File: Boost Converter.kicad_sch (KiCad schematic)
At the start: 21 parts, among them IC1 AHV85110KNHTR, J1 Array, J2 Battery, Q1 IGL65R080D2XUMA1, U1 Nucleo_L432KC

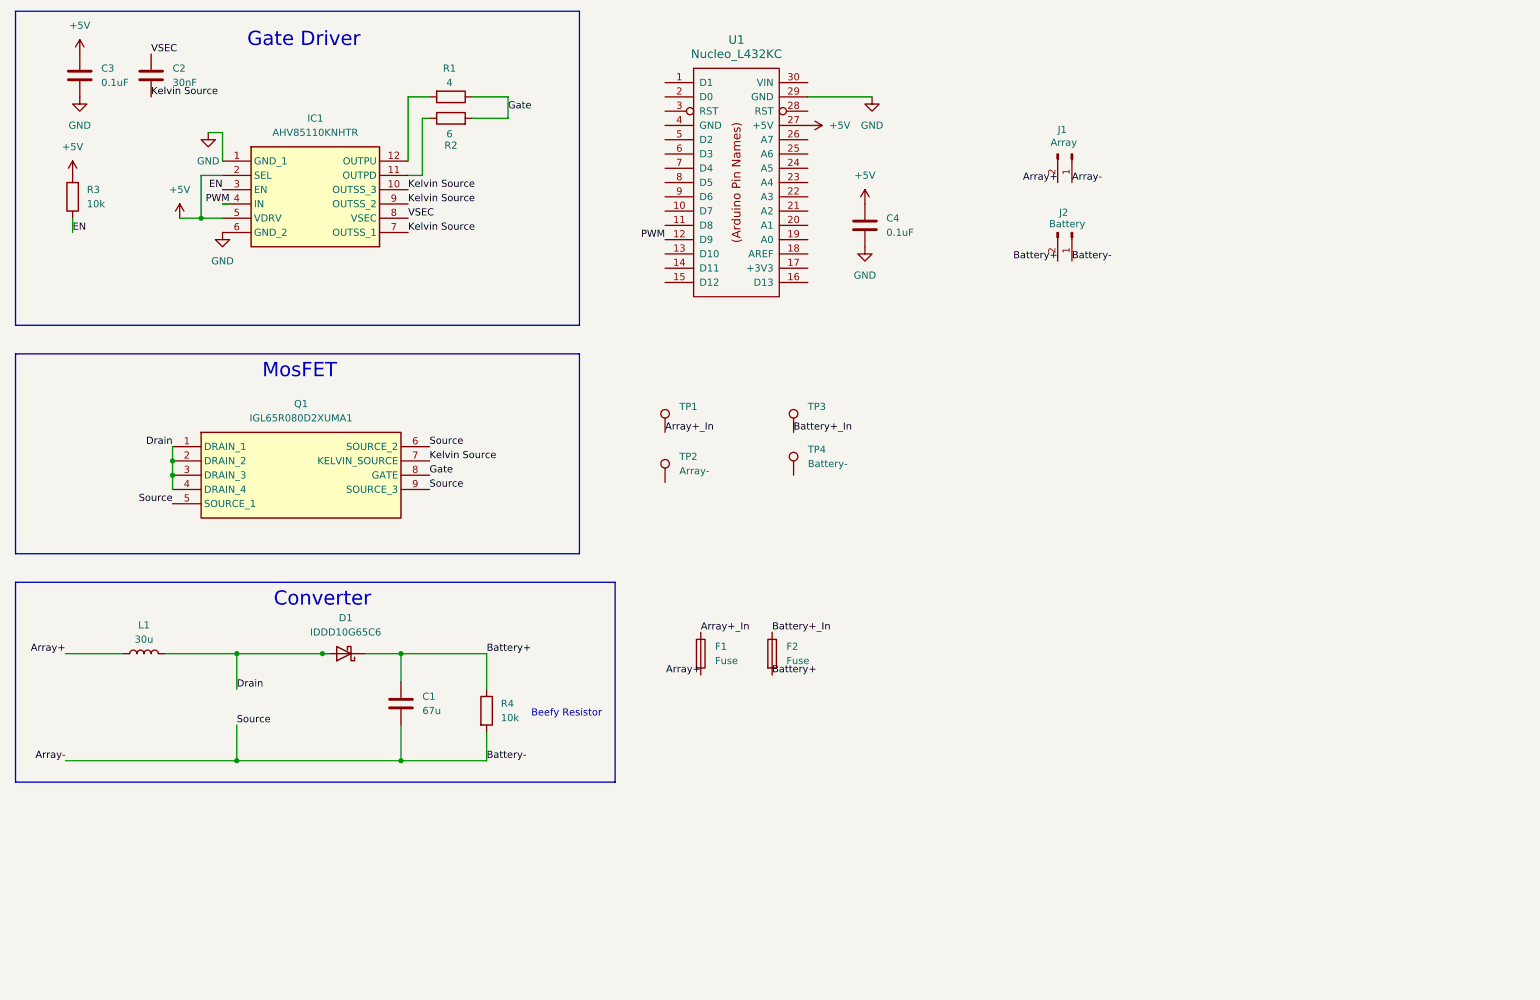
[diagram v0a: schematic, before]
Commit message: Changed Gan to MosFET. Added safety features. More test points. Changed gate driver to external power supply.
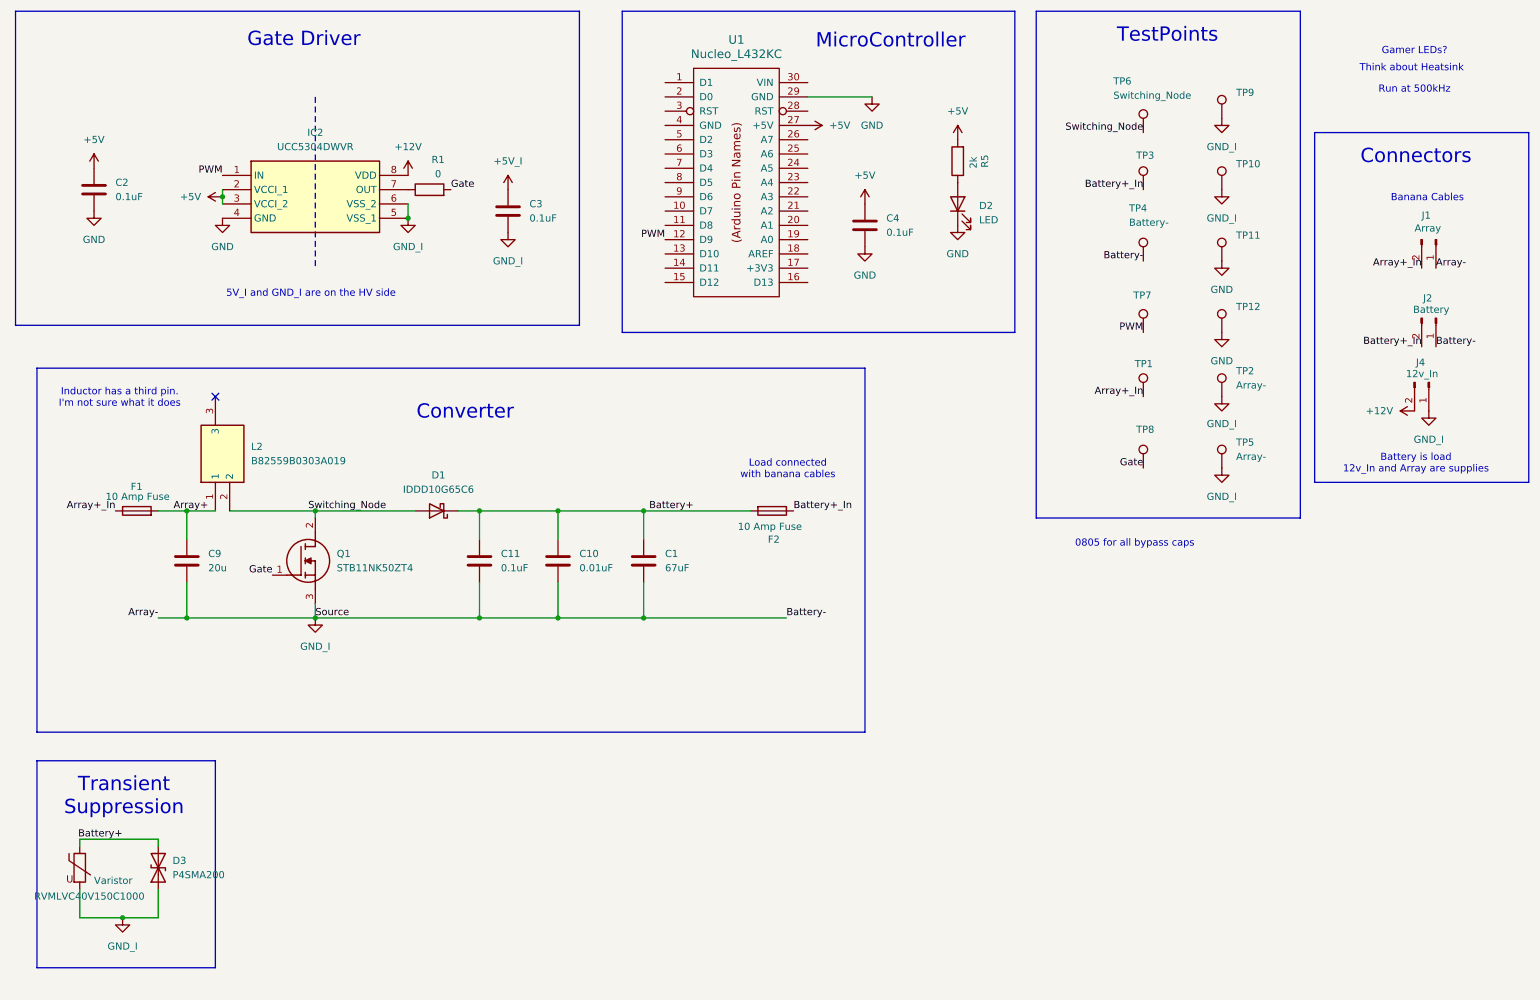
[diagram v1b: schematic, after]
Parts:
- removed IC1: AHV85110KNHTR, AHV85110KNHTR, symbol AHV85110KNHTR:AHV85110KNHTR
- removed L1: 30u, symbol Device:L
- removed Q1: IGL65R080D2XUMA1, IGL65R080D2XUMA1, symbol IGL65R080D2XUMA1:IGL65R080D2XUMA1
- removed R2: 6, symbol Device:R
- removed R3, R4: 10k, symbol Device:R
- added C10: 0.01uF, symbol Device:C
- added C11: 0.1uF, symbol Device:C
- added C9: 20u, symbol Device:C
- added D2: LED, symbol Device:LED
- added D3: P4SMA200, symbol Device:D_TVS
- added IC2: UCC5304DWVR, SOIC127P1150X280-8N, symbol UCC5304DWVR:UCC5304DWVR
- added J4: 12v_In, symbol Connector:Conn_01x02_Pin
- added L2: B82559B0303A019, B82559B0303A019, symbol B82559B0303A019:B82559B0303A019
- added Q1: STB11NK50ZT4, STB11NK50ZT4, symbol STB11NK50ZT4:STB11NK50ZT4
- added R5: 2k, symbol Device:R
- added RVMLVC40V150C1000: Varistor, symbol Device:Varistor
- added TP10, TP11, TP12, TP7, TP8, TP9: Array+, symbol Connector:TestPoint
- added TP5: Array-, symbol Connector:TestPoint
- added TP6: Switching_Node, symbol Connector:TestPoint
- C1: value 67u -> 67uF
- C2: value 30nF -> 0.1uF
- F1, F2: value Fuse -> 10 Amp Fuse
- R1: value 4 -> 0
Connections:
- net Array- is gone; now on net GND_I: C1.2, J1.1 (Pin_1), J2.1 (Pin_1)
- net Kelvin Source is gone; now on net GND: C2.2
- net VSEC is gone; now on net +5V: C2.1
- net +5V: now also IC2.2 (VCCI_1), IC2.3 (VCCI_2), R5.2; no longer C3.1
- net Array+: now also C9.1, L2.1; no longer J1.2 (Pin_2)
- net Array+_In: now also J1.2 (Pin_2)
- net Battery+: now also C10.1, C11.1, D3.2 (A2), RVMLVC40V150C1000.1; no longer J2.2 (Pin_2)
- net Battery+_In: now also J2.2 (Pin_2)
- net GND: now also D2.1 (K), IC2.4 (GND), TP11.1, TP12.1; no longer C3.2
- net Gate: now also R1.2, Q1.1 (G), TP8.1; no longer R1.1
- net PWM: now also IC2.1 (IN), TP7.1
- net GND_I: now reaches TP4.1
- net GND_I: now also C3.2, TP2.1, C10.2, C11.2, C9.2, D3.1 (A1), IC2.5 (VSS_1), IC2.6 (VSS_2), J4.1 (Pin_1), Q1.3 (S), RVMLVC40V150C1000.2, TP10.1, TP5.1, TP9.1
- net Drain renamed Switching_Node
- net Switching_Node: now also L2.2, Q1.2 (D), TP6.1
- new net: IC2.7 (OUT), R1.1
- new net: D2.2 (A), R5.1
- new net +12V: IC2.8 (VDD), J4.2 (Pin_2)
- new net +5V_I: C3.1
- no-connect marks 0 -> 1
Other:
- note added: "0805 for all bypass caps"
- note added: "5V_I and GND_I are on the HV side"
- note added: "Banana Cables"
- note added: "Battery is load 12v_In and Array are supplies"
- note added: "Connectors"
- note added: "Gamer LEDs?"
- note added: "Inductor has a third pin. I'm not sure what it does"
- note added: "Load connected with banana cables"
- note added: "MicroController"
- note added: "Run at 500kHz"
- note added: "TestPoints"
- note added: "Think about Heatsink"
- note added: "Transient Suppression"
- note removed: "Beefy Resistor"
- note removed: "MosFET"
- moved on the sheet: C1, D1, F1, F2, J1, J2, TP1, TP2, TP3, TP4

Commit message: Added varistor and tvs diode. Some other small changes.
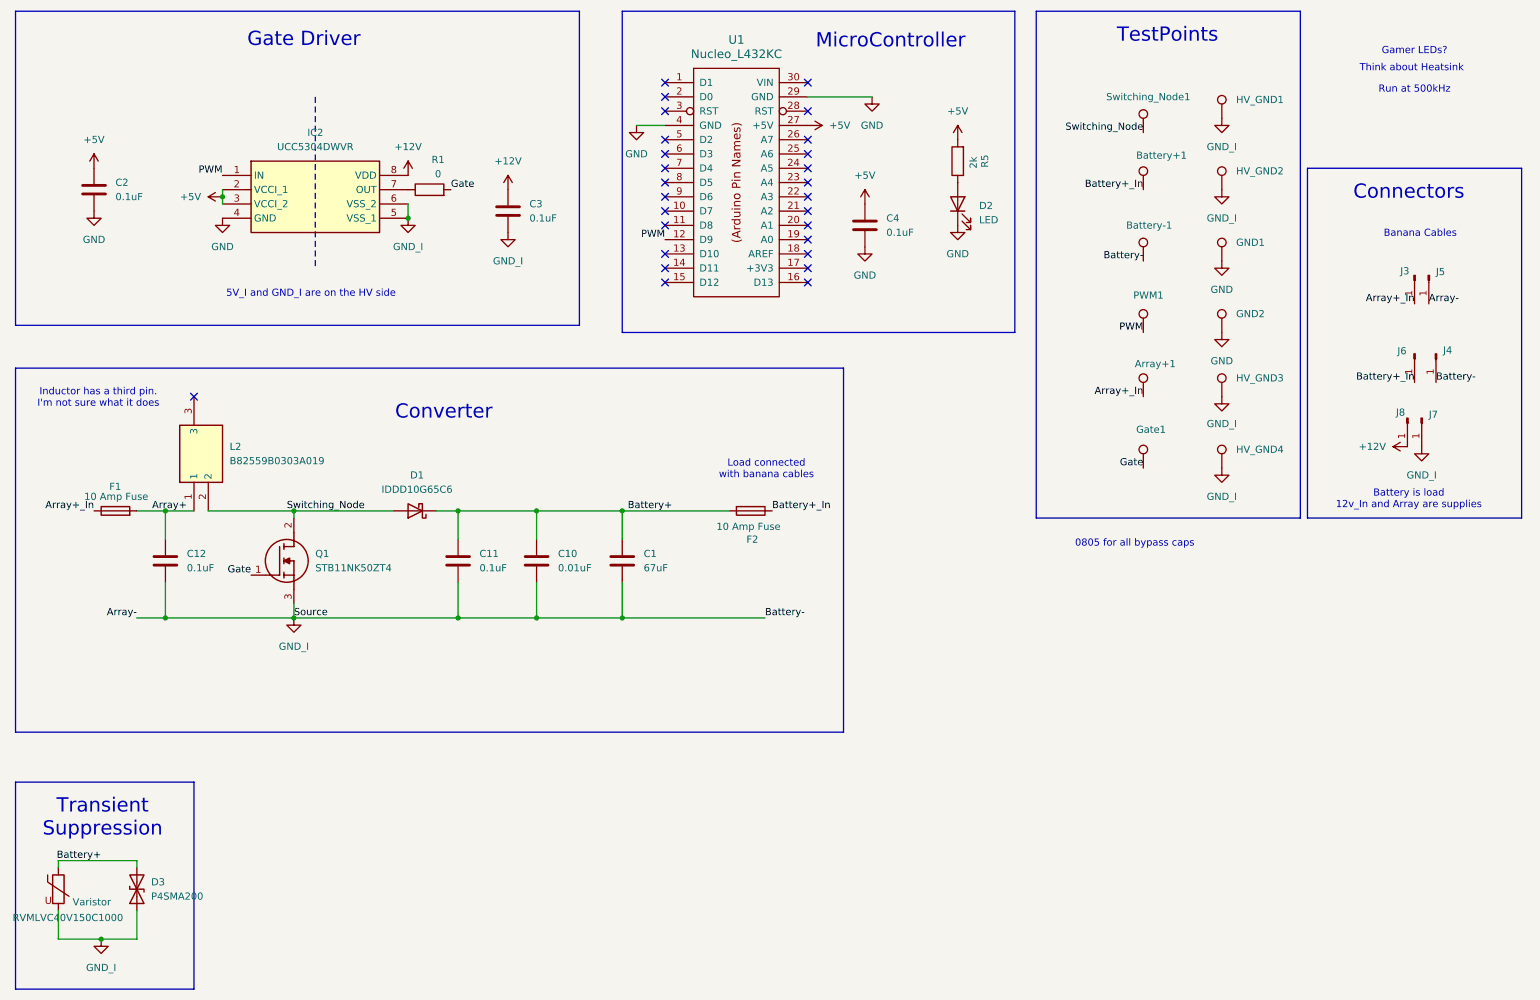
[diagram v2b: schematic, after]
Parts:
- removed C9: 20u, symbol Device:C
- removed J1: Array, symbol Connector:Conn_01x02_Pin
- removed J2: Battery, symbol Connector:Conn_01x02_Pin
- removed J4: 12v_In, symbol Connector:Conn_01x02_Pin
- added C12: 0.1uF, Capacitor_SMD:C_0805_2012Metric, symbol Device:C
- added J3, J4, J5, J6, J7, J8: Conn_01x01_Pin, 973582101:973582101, symbol Connector:Conn_01x01_Pin
- Array+1: renamed from TP1; footprint (none) -> TestPoint:TestPoint_Bridge_Pitch2.0mm_Drill0.7mm
- Battery+1: renamed from TP3; footprint (none) -> TestPoint:TestPoint_Bridge_Pitch2.0mm_Drill0.7mm
- Battery-1: renamed from TP4; footprint (none) -> TestPoint:TestPoint_Bridge_Pitch2.0mm_Drill0.7mm
- C1: footprint (none) -> Capacitor_THT:C_Disc_D6.0mm_W2.5mm_P5.00mm
- C10, C11, C2, C3, C4, R1, RVMLVC40V150C1000: footprint (none) -> Capacitor_SMD:C_0805_2012Metric
- D2: footprint (none) -> LED_SMD:LED_0805_2012Metric
- D3: footprint (none) -> Diode_SMD:D_SMA
- F1, F2: footprint (none) -> UTSVT_Passive:LittelFuse_OMNIBLOK_520Series_PCB
- GND1: renamed from TP11; footprint (none) -> TestPoint:TestPoint_Bridge_Pitch2.0mm_Drill0.7mm
- GND2: renamed from TP12; footprint (none) -> TestPoint:TestPoint_Bridge_Pitch2.0mm_Drill0.7mm
- Gate1: renamed from TP8; footprint (none) -> TestPoint:TestPoint_Bridge_Pitch2.0mm_Drill0.7mm
- HV_GND1: renamed from TP9; footprint (none) -> TestPoint:TestPoint_Bridge_Pitch2.0mm_Drill0.7mm
- HV_GND2: renamed from TP10; footprint (none) -> TestPoint:TestPoint_Bridge_Pitch2.0mm_Drill0.7mm
- HV_GND3: renamed from TP2; footprint (none) -> TestPoint:TestPoint_Bridge_Pitch2.0mm_Drill0.7mm
- HV_GND4: renamed from TP5; footprint (none) -> TestPoint:TestPoint_Bridge_Pitch2.0mm_Drill0.7mm
- IC2: footprint SOIC127P1150X280-8N -> UCC5304DWVR:SOIC127P1150X280-8N
- L2: footprint B82559B0303A019 -> B82559B0303A019:B82559B0303A019
- PWM1: renamed from TP7; footprint (none) -> TestPoint:TestPoint_Bridge_Pitch2.0mm_Drill0.7mm
- Q1: footprint STB11NK50ZT4 -> STB11NK50ZT4:STB11NK50ZT4
- R5: footprint (none) -> Resistor_SMD:R_0805_2012Metric
- Switching_Node1: renamed from TP6; footprint (none) -> TestPoint:TestPoint_Bridge_Pitch2.0mm_Drill0.7mm
- U1: footprint (none) -> UTSVT_Special:NucleoL432KC
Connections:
- net +5V_I is gone; now on net +12V: C3.1
- net +12V: now also J8.1 (Pin_1)
- net Array+: now also C12.1
- net Array+_In: now also J3.1 (Pin_1)
- net Battery+_In: now also J6.1 (Pin_1)
- net GND: now also U1.4 (GND)
- net GND_I: now also C12.2, J4.1 (Pin_1), J5.1 (Pin_1), J7.1 (Pin_1)
- no-connect marks 1 -> 27
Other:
- moved on the sheet: C1, C10, C11, D1, D3, F1, F2, L2, Q1, RVMLVC40V150C1000
